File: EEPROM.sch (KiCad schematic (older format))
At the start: 5 parts, among them IC1 M24M02-DRMN6TP

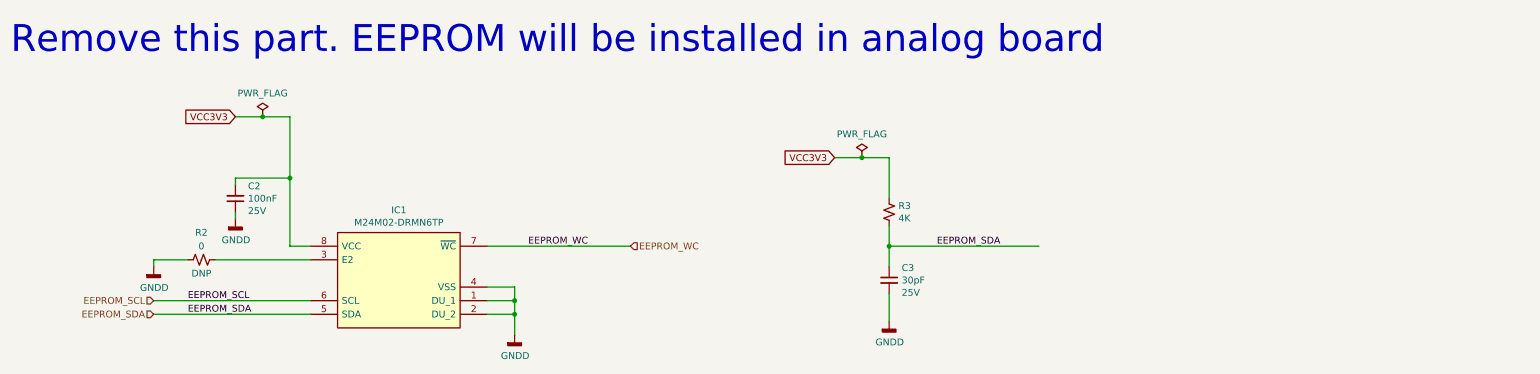
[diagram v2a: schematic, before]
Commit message: Corrected PCB import errors
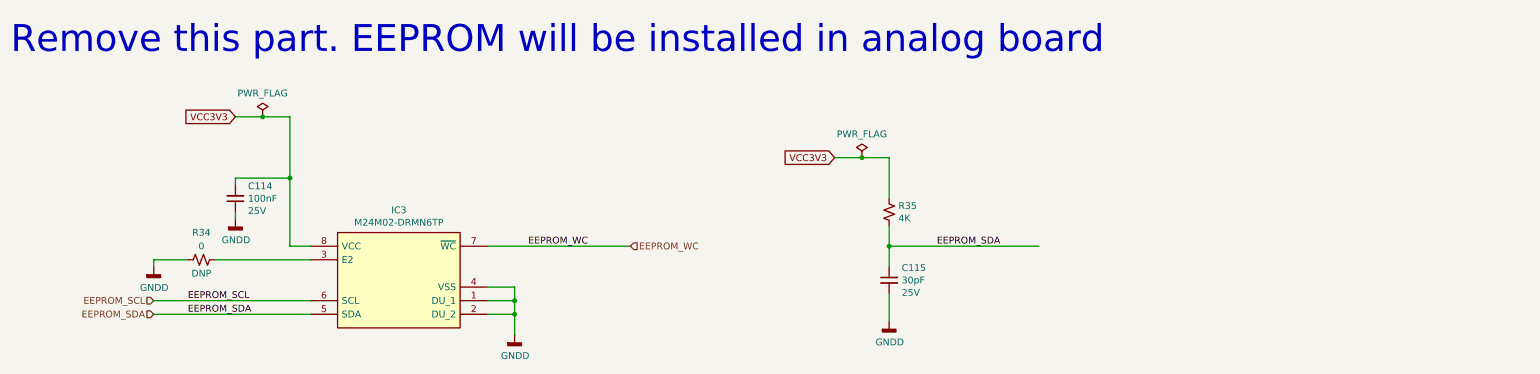
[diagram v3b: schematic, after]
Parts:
- renumbered C2 to C114, C3 to C115, IC1 to IC3, R2 to R34, R3 to R35
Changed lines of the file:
@@
 $EndDescr
 $Comp
-L GM_Memory_EEPROM:M24M02-DRMN6TP IC1
+L GM_Memory_EEPROM:M24M02-DRMN6TP IC3
 U 1 1 601D69D3
 P 3850 3300
-F 0 "IC1" H 4300 3465 50  0000 C CNN
+F 0 "IC3" H 4300 3465 50  0000 C CNN
 F 1 "M24M02-DRMN6TP" H 4300 3374 50  0000 C CNN
 F 2 "SOIC127P600X175-8N" H 5700 3500 50  0001 L CNN
@@
 P 5150 4050
 AR Path="/601DF0A6/601D83DB" Ref="#PWR?"  Part="1"
-AR Path="/601E7C5A/601D83DB" Ref="#PWR04"  Part="1"
-F 0 "#PWR04" H 5150 3800 50  0001 C CNN
+AR Path="/601E7C5A/601D83DB" Ref="#PWR046"  Part="1"
+F 0 "#PWR046" H 5150 3800 50  0001 C CNN
 F 1 "GNDD" H 5154 3895 50  0000 C CNN
 F 2 "" H 5150 4050 50  0001 C CNN
@@
 	3650 3900 2500 3900
 $Comp
-L Device:C_Small C2
+L Device:C_Small C114
 U 1 1 601DC16C
 P 3100 3050
-F 0 "C2" H 3008 2959 50  0000 R CNN
+F 0 "C114" H 3008 2959 50  0000 R CNN
 F 1 "100nF" H 3008 3050 50  0000 R CNN
 F 2 "Capacitor_SMD:C_0603_1608Metric_Pad1.08x0.95mm_HandSolder" H 3100 3050 50  0001 C CNN
@@
 P 3100 3200
 AR Path="/601DF0A6/601DF224" Ref="#PWR?"  Part="1"
-AR Path="/601E7C5A/601DF224" Ref="#PWR02"  Part="1"
-F 0 "#PWR02" H 3100 2950 50  0001 C CNN
+AR Path="/601E7C5A/601DF224" Ref="#PWR045"  Part="1"
+F 0 "#PWR045" H 3100 2950 50  0001 C CNN
 F 1 "GNDD" H 3104 3045 50  0000 C CNN
 F 2 "" H 3100 3200 50  0001 C CNN
@@
 	3500 2900 3500 3400
 $Comp
-L Device:R_Small_US R2
+L Device:R_Small_US R34
 U 1 1 601E53C9
 P 2850 3500
-F 0 "R2" V 3050 3500 50  0000 C CNN
+F 0 "R34" V 3050 3500 50  0000 C CNN
 F 1 "0" V 2950 3500 50  0000 C CNN
 F 2 "Resistor_SMD:R_0603_1608Metric_Pad0.98x0.95mm_HandSolder" H 2850 3500 50  0001 C CNN
@@
 P 2500 3550
 AR Path="/601DF0A6/601E70A9" Ref="#PWR?"  Part="1"
-AR Path="/601E7C5A/601E70A9" Ref="#PWR01"  Part="1"
-F 0 "#PWR01" H 2500 3300 50  0001 C CNN
+AR Path="/601E7C5A/601E70A9" Ref="#PWR044"  Part="1"
+F 0 "#PWR044" H 2500 3300 50  0001 C CNN
 F 1 "GNDD" H 2504 3395 50  0000 C CNN
 F 2 "" H 2500 3550 50  0001 C CNN
@@
 	2500 3500 2750 3500
 $Comp
-L Device:R_Small_US R3
+L Device:R_Small_US R35
 U 1 1 601EAD0F
 P 7900 3150
-F 0 "R3" H 7968 3196 50  0000 L CNN
+F 0 "R35" H 7968 3196 50  0000 L CNN
 F 1 "4K" H 7968 3105 50  0000 L CNN
 F 2 "Resistor_SMD:R_0603_1608Metric_Pad0.98x0.95mm_HandSolder" H 7900 3150 50  0001 C CNN
@@
 	7900 3400 7900 3550
 $Comp
-L Device:C_Small C3
+L Device:C_Small C115
 U 1 1 601EAD09
 P 7900 3650
-F 0 "C3" H 7992 3741 50  0000 L CNN
+F 0 "C115" H 7992 3741 50  0000 L CNN
 F 1 "30pF" H 7992 3650 50  0000 L CNN
 F 2 "Capacitor_SMD:C_0603_1608Metric_Pad1.08x0.95mm_HandSolder" H 7900 3650 50  0001 C CNN
@@
 P 7900 3950
 AR Path="/601DF0A6/601F091A" Ref="#PWR?"  Part="1"
-AR Path="/601E7C5A/601F091A" Ref="#PWR06"  Part="1"
-F 0 "#PWR06" H 7900 3700 50  0001 C CNN
+AR Path="/601E7C5A/601F091A" Ref="#PWR047"  Part="1"
+F 0 "#PWR047" H 7900 3700 50  0001 C CNN
 F 1 "GNDD" H 7904 3795 50  0000 C CNN
 F 2 "" H 7900 3950 50  0001 C CNN
@@
 VCC3V3
 $Comp
-L power:PWR_FLAG #FLG09
+L power:PWR_FLAG #FLG011
 U 1 1 60222E62
 P 3300 2450
-F 0 "#FLG09" H 3300 2525 50  0001 C CNN
+F 0 "#FLG011" H 3300 2525 50  0001 C CNN
 F 1 "PWR_FLAG" H 3300 2623 50  0000 C CNN
 F 2 "" H 3300 2450 50  0001 C CNN
@@
 VCC3V3
 $Comp
-L power:PWR_FLAG #FLG010
+L power:PWR_FLAG #FLG012
 U 1 1 602261D1
 P 7700 2750
-F 0 "#FLG010" H 7700 2825 50  0001 C CNN
+F 0 "#FLG012" H 7700 2825 50  0001 C CNN
 F 1 "PWR_FLAG" H 7700 2923 50  0000 C CNN
 F 2 "" H 7700 2750 50  0001 C CNN
